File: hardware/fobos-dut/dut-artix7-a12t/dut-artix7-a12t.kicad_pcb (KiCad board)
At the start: 4 copper layers, 88.9 x 76.2 mm, 182 parts, among them J1 Target, J2 Pmod 2x6, J3 575-8, J4 Glitch, J5 Conn_01x02, J6 Measure, J7 0878321420, J8 575-8, J9 Measure, Q1 FDS9435A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

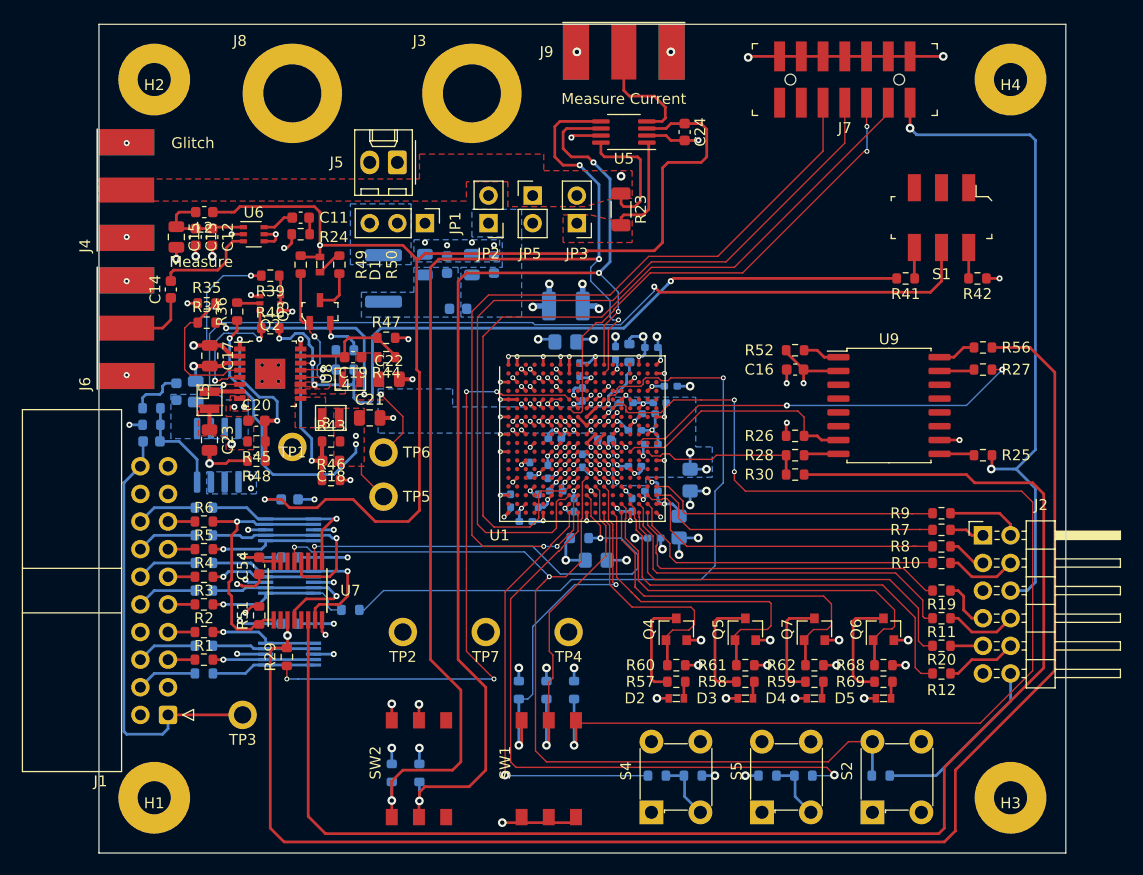
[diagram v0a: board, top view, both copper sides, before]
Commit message: Expanded copper pours on layer 3 Connected NC mux pins to the FPGA
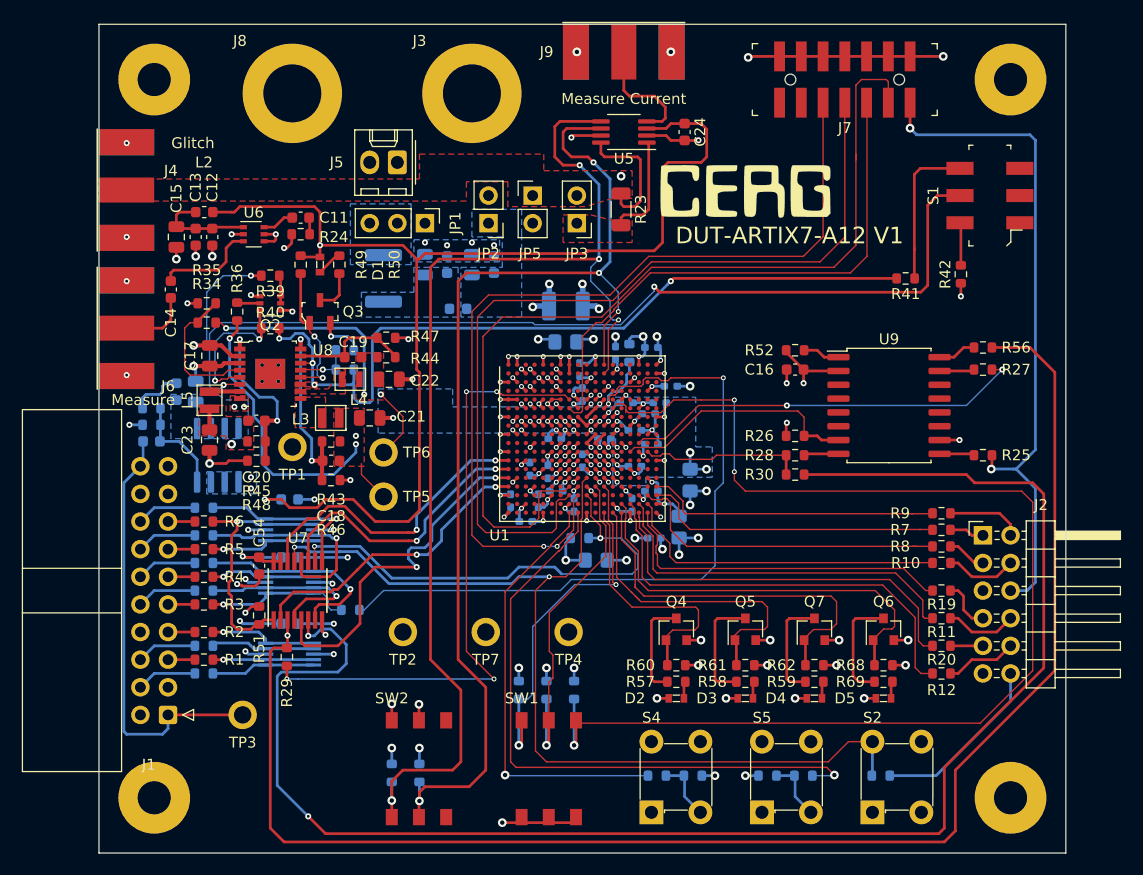
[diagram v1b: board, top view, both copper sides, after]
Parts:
- added G***: LOGO, cerg:cerg_logo, F.Cu at (59.4, 15.4)
- moved S1 4.89 mm to (81.9, 15.7), turned to 90 degrees
- moved R42 1.57 mm to (79.3, 23.0), turned to 90 degrees
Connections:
- U1 pad M1: Net-(U1-PadM1) -> FC_DIO2_MUX
- U1 pad N1: Net-(U1-PadN1) -> FC_DIO3_MUX
- U1 pad P1: Net-(U1-PadP1) -> FC_DIO1_MUX
- U1 pad R1: Net-(U1-PadR1) -> FC_DIO0_MUX
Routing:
- net FC_3V3: track 276.1 -> 134.9 mm
- net +3V3: track 252.8 -> 162.9 mm
- net VCCINT: track 102.1 -> 64.3 mm
- net FC_DIO1_MUX: track 0.00 -> 32.7 mm, vias 0 -> 2
- net FC_DIO2_MUX: track 0.00 -> 28.2 mm, vias 0 -> 2
- net FC_DIO0_MUX: track 0.00 -> 27.4 mm, vias 0 -> 2
- net FC_DIO3_MUX: track 0.00 -> 26.1 mm, vias 0 -> 2
- net Net-(J7-Pad4): track 74.5 -> 86.0 mm
- net Net-(R41-Pad1): track 2.85 -> 14.2 mm
- net SW_DIN: track 134.7 -> 145.1 mm, vias 0 -> 2
- net ON_OFF: track 81.1 -> 87.3 mm
- net Net-(J7-Pad6): track 46.1 -> 51.7 mm, vias 2 -> 0
- net Net-(J7-Pad8): track 74.8 -> 79.8 mm
- net Net-(J7-Pad10): track 77.2 -> 81.8 mm
- net Net-(R42-Pad2): track 2.85 -> 3.98 mm
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- added copper zone on In2.Cu, net FC_3V3
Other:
- board text added: "DUT-ARTIX7-A12 V1"

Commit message: Added external 5V connector Added shunt for FC3v3 and 3V3 Added silkscreen which clarifies switch functionality Thickened 5 mil traces to 7 mil where feasible Moved Vcore amplifier closer to Vcore pad to reduce amplification of noise
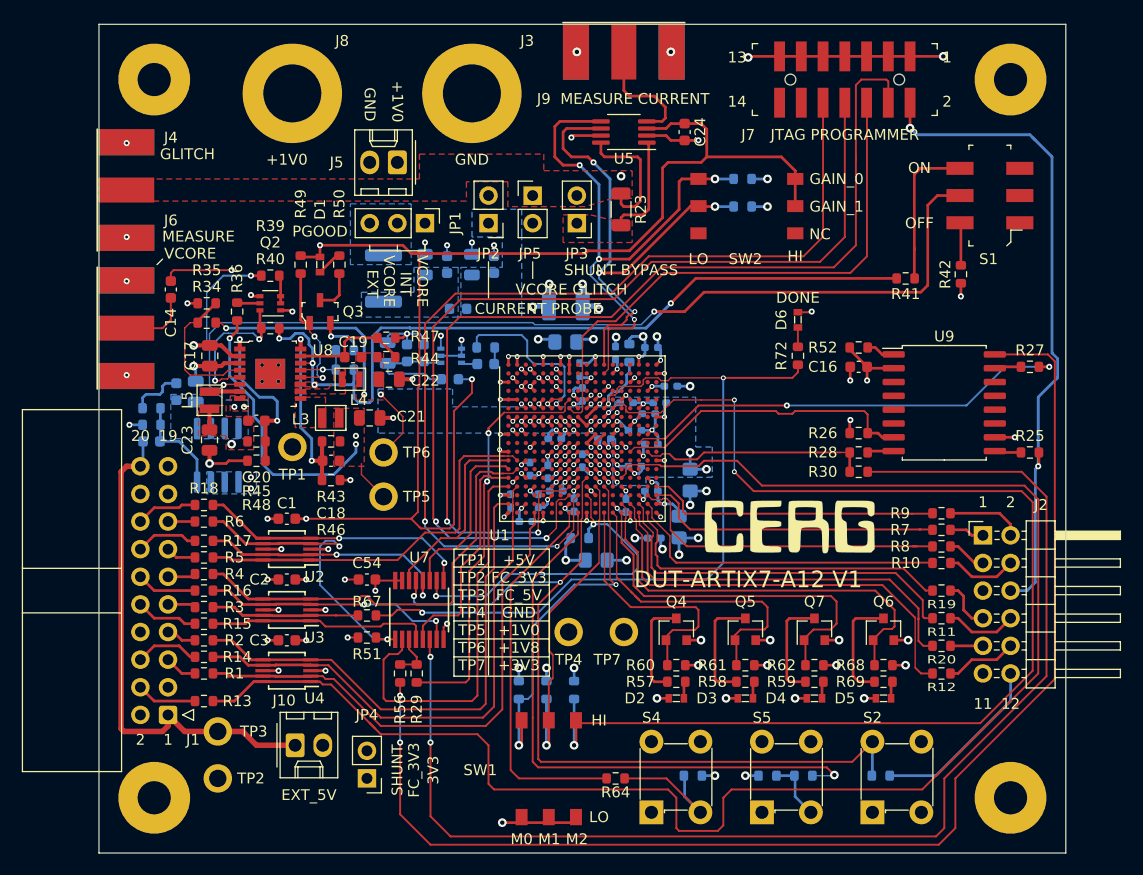
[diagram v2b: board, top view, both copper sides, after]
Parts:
- added D6: LG_L29K-G2J1-24-Z, digikey-footprints:0603, F.Cu at (64.3, 27.2)
- added J10: Conn_01x02, Connector_Molex:Molex_KK-254_AE-6410-02A_1x02_P2.54mm_Vertical, F.Cu at (18.0, 66.3)
- added JP4: FC3V3_3V3_SHUNT, Connector_PinHeader_2.54mm:PinHeader_1x02_P2.54mm_Vertical, F.Cu at (24.6, 69.3)
- added R72: 200R, Resistor_SMD:R_0603_1608Metric, F.Cu at (64.3, 30.5)
- C1, C2, C3, R13, R14, R15, R16, R17, R18, R64, R67, U2, U3, U4: moved to F.Cu
- C11, C12, C13, C15, L2, R24, U6: moved to B.Cu
- R53: value 330R -> 200R
- moved SW2 65.1 mm to (55.1, 14.2), turned to 0 degrees
- moved R70 63.4 mm to (59.2, 14.2), turned to 180 degrees
- moved R56 61.4 mm to (27.7, 59.7), turned to 270 degrees
- moved R71 60.0 mm to (59.2, 16.8), turned to 180 degrees
- moved G*** 31.1 mm to (63.5, 46.2)
- moved L2 27.3 mm to (32.3, 32.6)
- moved C12 22.2 mm to (29.8, 30.2), turned to 90 degrees
- moved C15 22.2 mm to (26.5, 30.2), turned to 90 degrees
- moved C13 22.2 mm to (28.3, 30.2), turned to 90 degrees
- moved C11 21.7 mm to (35.6, 31.2)
- moved TP2 21.7 mm to (10.9, 69.3)
- moved U6 21.3 mm to (32.4, 30.5)
- moved R24 20.0 mm to (35.6, 29.7)
- moved TP7 12.7 mm to (48.3, 55.9)
- moved R29 12.0 mm to (29.2, 59.7)
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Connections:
- U1 pad M2: Net-(U1-PadM2) -> FD2C_HS
- U1 pad N2: Net-(U1-PadN2) -> FC2D_HS
- U1 pad P14: Net-(U1-PadP14) -> FD2C_CLK
- U1 pad R2: Net-(U1-PadR2) -> FC2D_CLK
- U1 pad U1: Net-(U1-PadU1) -> FC_IO
- U1 pad V4: Net-(U1-PadV4) -> FC_RST
- U3 pad 1: FD_TF -> FC_DIO0
- U3 pad 10: FD_TF -> FC_DIO0
- U3 pad 2: FC_DIO0 -> FD_TF
- U3 pad 4: FC2D_HS -> FC_DIO1
- U3 pad 5: FC_DIO1 -> FC2D_HS
- U3 pad 6: FC_DIO1 -> FC2D_HS
- U3 pad 7: FC2D_HS -> FC_DIO1
- U3 pad 9: FC_DIO0 -> FD_TF
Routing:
- net FD2C_CLK: track 9.57 -> 151.2 mm
- net SW_CLK: track 137.1 -> 4.13 mm, vias 1 -> 0
- net Net-(R56-Pad2): track 3.53 -> 117.5 mm, vias 0 -> 2
- net VCORE_CURRENT_GAIN_0: track 107.0 -> 51.5 mm
- net VCORE_CURRENT_GAIN_1: track 100.2 -> 47.1 mm
- net FC2D_CLK: track 9.57 -> 49.7 mm
- net FC_RST: track 9.25 -> 48.6 mm, vias 1 -> 0
- net FC_IO: track 9.91 -> 47.7 mm, vias 1 -> 0
- net FC2D_HS: track 9.64 -> 40.1 mm, vias 1 -> 0
- net SW_DIN: track 145.1 -> 116.8 mm
- net FD2C_HS: track 9.81 -> 35.8 mm, vias 1 -> 0
- net Net-(C14-Pad2): track 9.37 -> 30.3 mm, vias 0 -> 2
- net Net-(R29-Pad2): track 57.5 -> 37.7 mm, vias 4 -> 2
- net VCCINT: track 64.3 -> 49.2 mm, vias 23 -> 22
- net SW_INIT_B: track 44.2 -> 32.2 mm
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- removed copper zone on In1.Cu, net (none)
- removed copper zone on B.Cu, net GND
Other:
- board text added: "+1V0"
- board text added: "+5V FC_3V3 FC_5V GND +1V0 +1V8 +3V3"
- board text added: "1"
- board text added: "11"
- board text added: "12"
- board text added: "13"
- board text added: "14"
- board text added: "19"
- board text added: "2"
- board text added: "20"
- board text added: "3V3"
- board text added: "CURRENT PROBE"
- board text added: "DONE"
- board text added: "EXT"
- board text added: "EXT_5V"
- board text added: "FC_3V3"
- board text added: "GAIN_0"
- board text added: "GAIN_1"
- board text added: "GLITCH"
- board text added: "GND"
- board text added: "HI"
- board text added: "INT"
- board text added: "JTAG PROGRAMMER"
- board text added: "LO"
- board text added: "M0"
- board text added: "M1"
- board text added: "M2"
- board text added: "MEASURE"
- board text added: "MEASURE CURRENT"
- board text added: "NC"
- board text added: "OFF"
- board text added: "ON"
- board text added: "PGOOD"
- board text added: "SHUNT"
- board text added: "SHUNT BYPASS"
- board text added: "TP1 TP2 TP3 TP4 TP5 TP6 TP7"
- board text added: "VCORE"
- board text added: "VCORE GLITCH"
- board text removed: "Glitch"
- board text removed: "Measure"
- board text removed: "Measure Current"

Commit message: Added Manufacturer Part Number, Manufacturer to all components except ferrite beads Added digikey quote
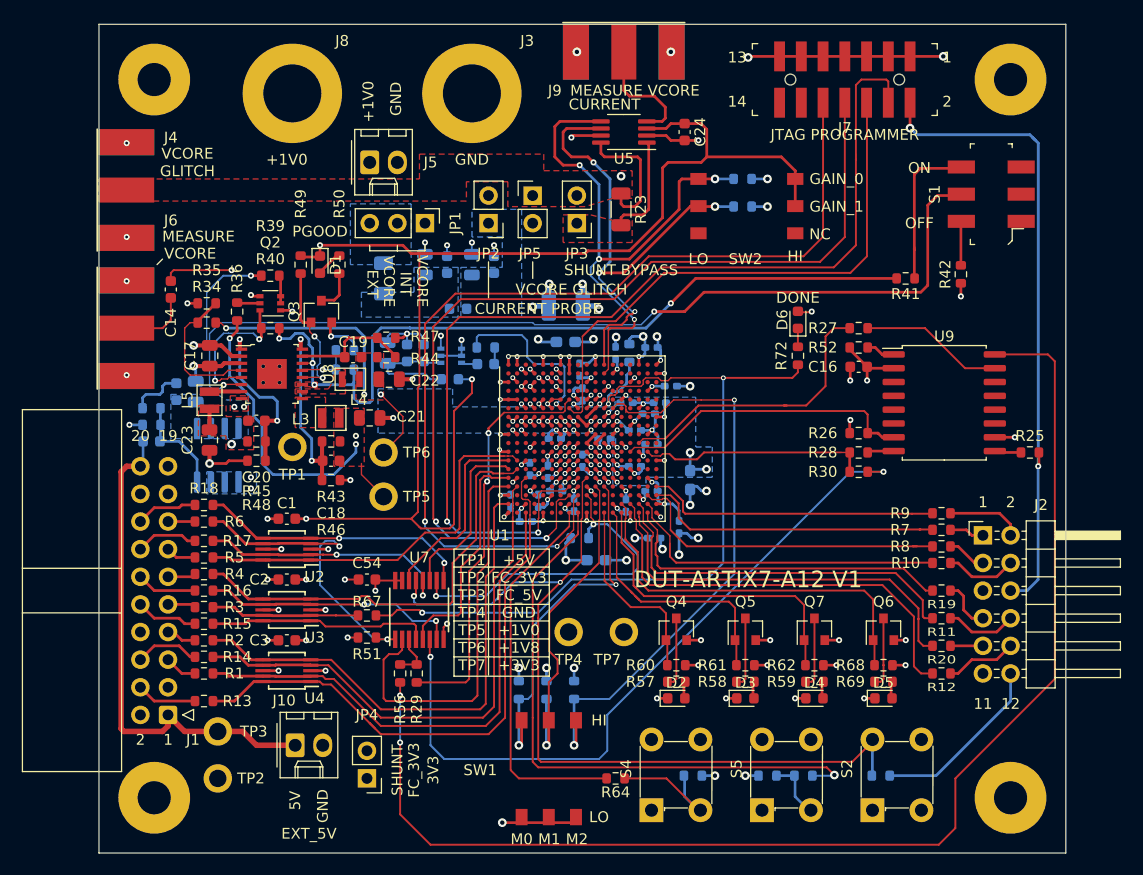
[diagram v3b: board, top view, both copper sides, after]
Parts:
- removed G***: LOGO, cerg:cerg_logo
- C16: value 100n -> 100nF
- C25: footprint Resistor_SMD:R_1210_3225Metric_Pad1.30x2.65mm_HandSolder -> Capacitor_SMD:C_1210_3225Metric_Pad1.33x2.70mm_HandSolder
- C26, C27, C35: footprint Resistor_SMD:R_0805_2012Metric_Pad1.20x1.40mm_HandSolder -> Capacitor_SMD:C_0603_1608Metric_Pad1.08x0.95mm_HandSolder
- C28, C29, C30, C31, C32, C33, C34, C37, C38, C39, C40, C41, C42, C43, C44, C45, C46, C47, C48, C49, C50, C51, C52, C53: footprint Resistor_SMD:R_0402_1005Metric_Pad0.72x0.64mm_HandSolder -> Capacitor_SMD:C_0402_1005Metric_Pad0.74x0.62mm_HandSolder
- C36: footprint Resistor_SMD:R_0805_2012Metric_Pad1.20x1.40mm_HandSolder -> Capacitor_SMD:C_0402_1005Metric_Pad0.74x0.62mm_HandSolder
- D1, D2, D3, D4, D5, D6: footprint digikey-footprints:0603 -> LED_SMD:LED_0603_1608Metric
- F1: footprint Fuse:Fuse_1812_4532Metric -> Fuse:Fuse_1206_3216Metric
- J7: footprint digikey-footprints:PinHeader_2x7_P2mm_SMD -> cerg:PinHeader_2x7_P2mm_SMD
- Q3: value FDV301N -> BSS138; footprint digikey-footprints:SOT-23-3 -> Package_TO_SOT_SMD:SOT-23
- R37: value 0 -> 0R
- S1: footprint digikey-footprints:Switch_Slide_JS202011SCQN -> cerg:Switch_Slide_JS202011SCQN
- S2, S4, S5: footprint digikey-footprints:Switch_Tactile_THT_6x6mm -> cerg:Switch_Tactile_THT_6x6mm
- U8: footprint digikey-footprints:TSSOP-16-1EP_W4.40mm -> cerg:TSSOP-16-1EP_W4.40mm
- moved R27 16.1 mm to (69.9, 27.9), turned to 0 degrees
- moved J5 2.54 mm to (24.9, 12.7), turned to 0 degrees
- moved S2 0.20 mm to (71.1, 72.3)
- moved S4 0.20 mm to (50.8, 72.3)
- moved S5 0.20 mm to (61.0, 72.3)
- moved S1 0.18 mm to (82.0, 15.6)
- moved U8 0.16 mm to (15.9, 32.1)
- moved Q3 0.13 mm to (20.5, 26.4)
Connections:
- U1 pad P14: FD2C_CLK -> Net-(U1-PadP14)
- U1 pad P3: Net-(U1-PadP3) -> FD2C_CLK
- U1 pad V3: Net-(U1-PadV3) -> FC_RST
- U1 pad V4: FC_RST -> Net-(U1-PadV4)
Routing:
- net FD2C_CLK: track 151.2 -> 54.7 mm
- net Net-(R33-Pad2): track 113.5 -> 54.6 mm, vias 3 -> 2
- net SW_DIN: track 116.8 -> 66.3 mm
- net Net-(R27-Pad1): track 41.6 -> 26.7 mm, vias 2 -> 0
- net Net-(R27-Pad2): track 2.46 -> 13.2 mm
- net USER_LED_1: track 23.6 -> 18.0 mm
- net USER_LED_2: track 29.7 -> 24.1 mm
- net USER_LED_3: track 34.6 -> 29.2 mm
- net Net-(Q5-Pad3): track 10.3 -> 6.51 mm
- net Net-(Q6-Pad3): track 10.2 -> 6.51 mm
- net Net-(Q7-Pad3): track 9.79 -> 6.51 mm
- net Net-(Q4-Pad3): track 9.28 -> 6.51 mm
- net USER_LED_4: track 38.8 -> 36.2 mm
- net GND: track 200.2 -> 202.3 mm
- net +3V3: track 160.2 -> 159.6 mm
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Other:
- board text added: "5V"
- board text added: "CURRENT"
- board text added: "MEASURE VCORE"
- board text removed: "GLITCH"
- board text removed: "MEASURE CURRENT"
